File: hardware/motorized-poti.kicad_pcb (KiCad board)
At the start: 2 copper layers, 130 x 20 mm, 30 parts, among them J101 Debug, P1 CON-SENSOR2, P2 MOTORIZED_POTI, P3 BOOT, U1 XMC1100-16, U101 TLV271IDBVR, U2 ZXBM5210, U3 DRILL, U4 DRILL, U5 DRILL, U6 DRILL

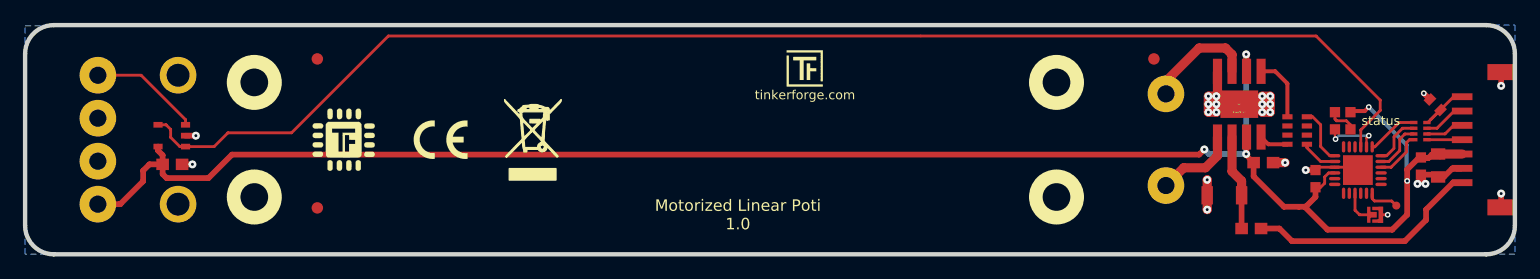
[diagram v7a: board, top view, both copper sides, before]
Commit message: Change capacitor footprint(s) to C0402F
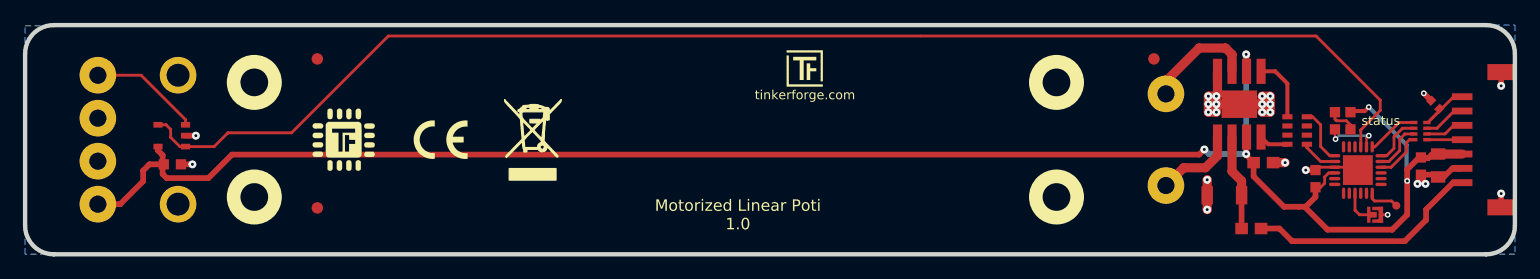
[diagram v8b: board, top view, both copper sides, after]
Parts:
- C101: footprint kicad-libraries:C0603E -> kicad-libraries:C0603F
- C2: footprint C0805 -> kicad-libraries:C0805
- C4, C5: footprint C0603F -> kicad-libraries:C0603F
- C6: footprint C0402E -> kicad-libraries:C0402F
- D1: footprint D0603F -> kicad-libraries:D0603F
- J101: footprint DEBUG_PAD -> kicad-libraries:DEBUG_PAD
- L1: footprint C0603E -> kicad-libraries:C0603E
- P1: footprint CON-SENSOR2 -> kicad-libraries:CON-SENSOR2
- R1: footprint R0603F -> kicad-libraries:R0603F
- RP1: footprint 4X0603 -> kicad-libraries:4X0603
- U2: footprint SO-8-EP -> kicad-libraries:SO-8-EP
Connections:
- P2 pad 2: (no net) -> Net-(P2-Pad2)
- RP1 pad 2: (no net) -> Net-(RP1-Pad2)
- RP1 pad 3: (no net) -> Net-(RP1-Pad3)
- RP1 pad 6: (no net) -> Net-(RP1-Pad6)
- RP1 pad 7: (no net) -> Net-(RP1-Pad7)
- U1 pad 11: (no net) -> Net-(U1-Pad11)
- U1 pad 12: (no net) -> Net-(U1-Pad12)
- U1 pad 13: (no net) -> Net-(U1-Pad13)
- U1 pad 14: (no net) -> Net-(U1-Pad14)
- U1 pad 16: (no net) -> Net-(U1-Pad16)
- U1 pad 17: (no net) -> Net-(U1-Pad17)
- U1 pad 19: (no net) -> Net-(U1-Pad19)
- U1 pad 20: (no net) -> Net-(U1-Pad20)
- U1 pad 21: (no net) -> Net-(U1-Pad21)
- U1 pad 4: (no net) -> Net-(U1-Pad4)
- U1 pad 5: (no net) -> Net-(U1-Pad5)
- U1 pad 6: (no net) -> Net-(U1-Pad6)
